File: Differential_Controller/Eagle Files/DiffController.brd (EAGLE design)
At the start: 55.5 x 60.9 mm, 9 parts, among them J1 1990083, J2 1990083, U1 L7805CV

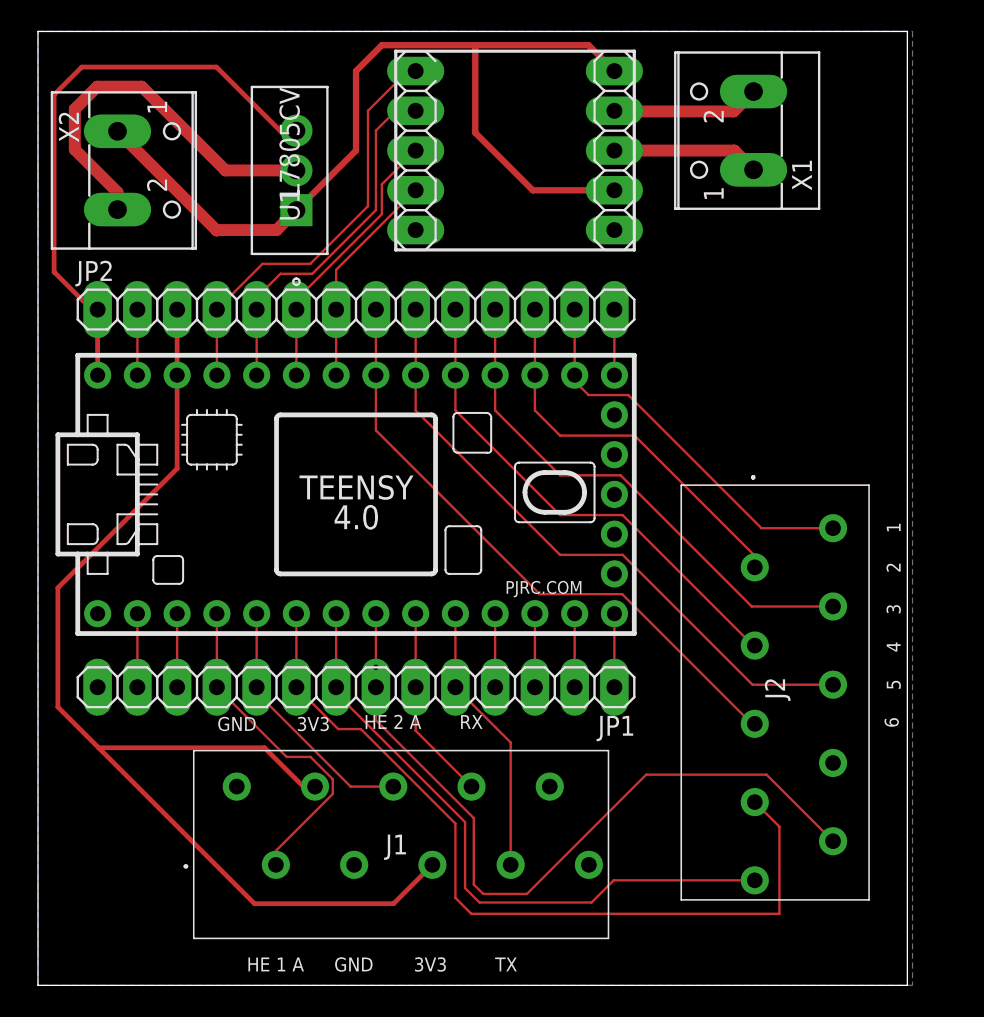
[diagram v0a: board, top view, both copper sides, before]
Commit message: Fixed diff controller PCB
Made the traces bigger to handle more current and moved M_OUT_NEG to actually connect to Teensy
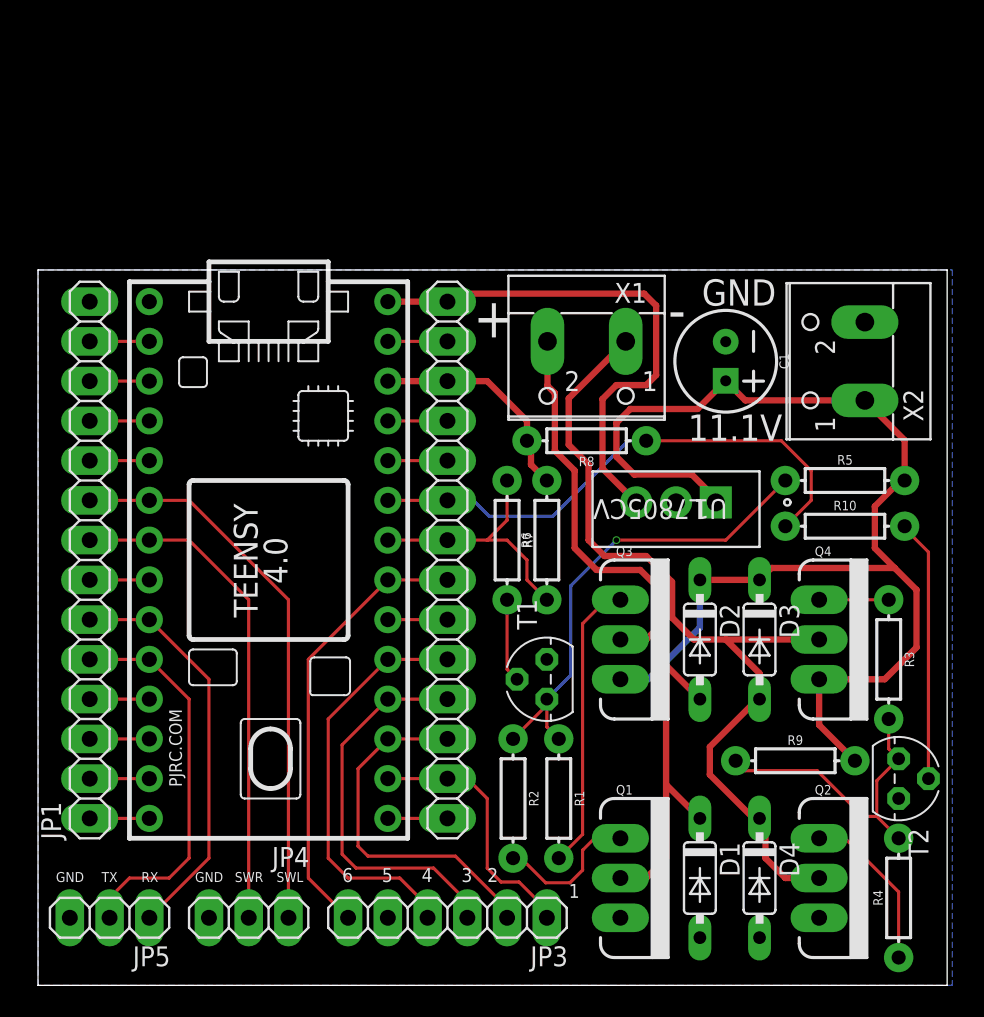
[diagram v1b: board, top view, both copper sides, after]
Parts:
- removed J1, J2: 1990083, 1990083:1990083
- removed U$2: TEENSY_4.0_EXPANDED_1, Microcontroller:TEENSY_4.0_EXPANDED_1
- added C1: 100uF, SparkFun-Capacitors:CPOL-RADIAL-2.5MM-6.5MM
- added D1, D2, D3, D4: 1N4148DO35-7, diode:DO35-7
- added JP3: (no value), GTOR - Connectors:1X06
- added JP4, JP5: (no value), GTOR - Connectors:1X03
- added Q1, Q2: 60V/32A/35mΩ, SparkFun-DiscreteSemi:TO220V
- added Q3, Q4: 24A/20V/50mΩ, SparkFun-DiscreteSemi:TO220V
- added R1, R2, R3, R4: 100Ω, SparkFun-Resistors:AXIAL-0.3
- added R10, R7: 1kΩ, SparkFun-Resistors:AXIAL-0.3
- added R5, R6, R8, R9: 10kΩ, SparkFun-Resistors:AXIAL-0.3
- added T1, T2: BC337, transistor:TO92
- U$1: value MAX14870_BREAKOUT -> TEENSY_4.0_SIMPLE; device Breakout Boards:MAX14870_BREAKOUT -> GTOR - Microcontroller:TEENSY_4.0_SIMPLE
- moved X2 46.8 mm to (51.6, 41.1), turned to 90 degrees
- moved U1 32.7 mm to (43.3, 32.1), turned to 180 degrees
- moved U$1 21.4 mm to (14.7, 28.4), turned to 270 degrees
- moved JP1 18.9 mm to (3.30, 28.4), turned to 90 degrees
- moved X1 17.5 mm to (35.1, 41.1), turned to 180 degrees
- moved JP2 17.0 mm to (26.2, 28.4), turned to 270 degrees
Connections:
- removed net DIG1: J2.1, JP2.13, U$2.14/A0
- removed net DIG2: J2.2, JP2.12, U$2.15/A1
- removed net DIG3: J2.3, JP2.11, U$2.16/A2
- removed net DIG4: J2.4, JP2.10, U$2.17/A3
- removed net DIG5: J2.5, JP2.9, U$2.18/A4/SDA
- removed net DIG6: J2.6, JP2.8, U$2.19/A5/SCL
- removed net DIG7: J2.8, JP1.9, U$2.4/CANRX
- removed net DIG8: J2.10, JP1.8, U$2.5
- removed net DIG9: J2.9, JP1.7, U$2.6
- removed net DIR: JP2.5, U$1.DIR, U$2.22/A8
- removed net HE1_A: J1.2, JP1.11, U$2.2
- removed net HE2_A: J1.5, JP1.10, U$2.3/CANTX
- removed net NEN: JP2.7, U$1.NEN, U$2.20/A6
- removed net NFAULT: JP2.6, U$1.NFAULT, U$2.21/A7
- removed net PWM: JP2.4, U$1.PWM, U$2.23/A9
- new net DIFF1: JP2.13, JP3.1, U$1.14/A0
- new net DIFF2: JP2.12, JP3.2, U$1.15/A1
- new net DIFF3: JP2.11, JP3.3, U$1.16/A2
- new net DIFF4: JP2.10, JP3.4, U$1.17/A3
- new net DIFF6: JP2.8, JP3.6, U$1.19/A5/SCL
- new net M_IN_NEG: JP2.6, R10.P$1, R8.P$1, U$1.21/A7
- new net M_IN_POS: JP2.7, R6.P$1, R7.P$1, U$1.20/A6
- new net M_OUT_NEG: D3.A, D4.C, Q2.2, Q4.2, X1.1
- new net M_OUT_POS: D1.C, D2.A, Q1.2, Q3.2, X1.2
- new net N$11: JP1.7, U$1.6
- new net N$12: JP2.5, U$1.22/A8
- new net N$13: Q1.1, R2.P$2
- new net N$14: Q2.1, R4.P$1
- new net N$15: Q3.1, R1.P$2
- new net N$16: Q4.1, R3.P$1
- new net N$17: R3.P$2, R4.P$2, R9.P$1, T2.3
- new net N$18: R7.P$2, T1.2
- new net N$19: R1.P$1, R2.P$1, R5.P$1, T1.3
- new net N$20: R10.P$2, T2.2
- new net N$21: JP1.11, U$1.2
- new net N$22: JP1.10, U$1.3/CANTX
- new net SWITCH_LEFT: JP1.9, JP4.1, U$1.4/CANRX
- new net SWITCH_RIGHT: JP1.8, JP4.2, U$1.5
- net 3V3: now also R6.P$2, R8.P$2, U$1.3V3_LO; no longer J1.3, J1.6, U$2.3V3_LO
- net 5V: now also U$1.VIN; no longer U$2.VIN
- net GND: now also C1.2, D1.A, D4.A, JP3.5, JP4.3, JP5.3, Q1.3, Q2.3, T1.1, T2.1, U$1.GND; no longer J1.1, J1.4, U$1.GND_BRD, U$1.GND_MCU, U$2.GND
- net N$1: now also JP2.9, U$1.18/A4/SDA; no longer U$1.M1, X1.2
- net N$10: now also U$1.13/SCK; no longer U$2.13/SCK
- net N$2: now also JP2.4, U$1.23/A9; no longer U$1.M2, X1.1
- net N$3: now also U$1.0/RX; no longer U$2.0/RX
- net N$4: now also U$1.1/TX; no longer U$2.1/TX
- net N$5: now also U$1.GND2; no longer U$2.GND2
- net N$6: now also U$1.9/CS; no longer U$2.9/CS
- net N$7: now also U$1.10/CS; no longer U$2.10/CS
- net N$8: now also U$1.11/MOSI; no longer U$2.11/MOSI
- net N$9: now also U$1.12/MISO; no longer U$2.12/MISO
- net RX: now also JP5.1, U$1.7; no longer J1.7, U$2.7
- net TX: now also JP5.2, U$1.8; no longer J1.8, U$2.8
- net VBAT: now also C1.1, D2.C, D3.C, Q3.3, Q4.3, R5.P$2, R9.P$2; no longer U$1.VIN, U$1.VM
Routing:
- net 3V3: track 73.6 -> 14.3 mm
- net M_OUT_NEG: track 0.00 -> 55.3 mm
- net DIG7: track 52.1 -> 0.00 mm
- net M_OUT_POS: track 0.00 -> 50.1 mm
- net DIG9: track 49.3 -> 0.00 mm, vias 1 -> 0
- net DIG8: track 40.4 -> 0.00 mm
- net DIG5: track 40.4 -> 0.00 mm
- net DIG6: track 39.7 -> 0.00 mm
- net SWITCH_LEFT: track 0.00 -> 35.7 mm
- net M_IN_NEG: track 0.00 -> 34.5 mm
- net DIG3: track 33.2 -> 0.00 mm
- net SWITCH_RIGHT: track 0.00 -> 32.1 mm
- net DIG4: track 31.8 -> 0.00 mm
- net N$19: track 0.00 -> 30.7 mm, vias 0 -> 1
- net DIFF6: track 0.00 -> 28.6 mm
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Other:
- board size 55.5 x 60.9 mm -> 58.1 x 45.7 mm
- board text added: "+"
- board text added: "-"
- board text added: "11.1V"
- board text added: "SWL"
- board text added: "SWR"
- board text removed: "3V3"
- board text removed: "Differential Controller Board GT Off-Road | Evelyn Craven"
- board text removed: "HE 1 A"
- board text removed: "HE 2 A"
